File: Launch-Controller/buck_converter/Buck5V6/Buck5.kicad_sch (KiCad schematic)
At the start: 13 parts, among them J1 Conn_01x10_Socket, U1 LM2596S-5

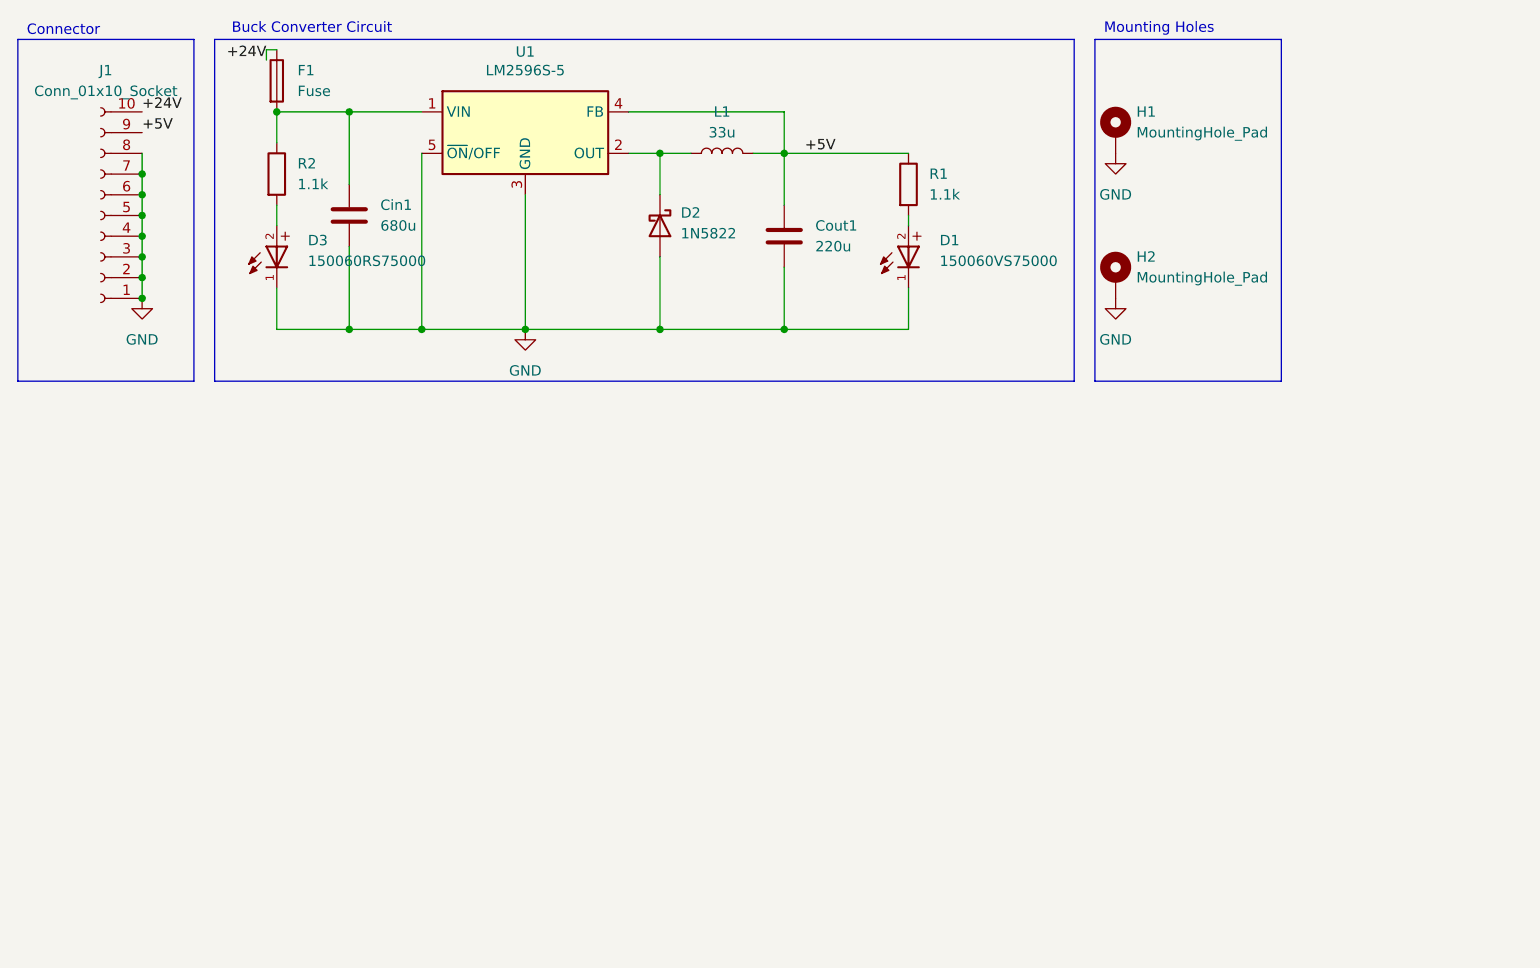
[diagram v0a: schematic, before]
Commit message: buck converter v2 changes
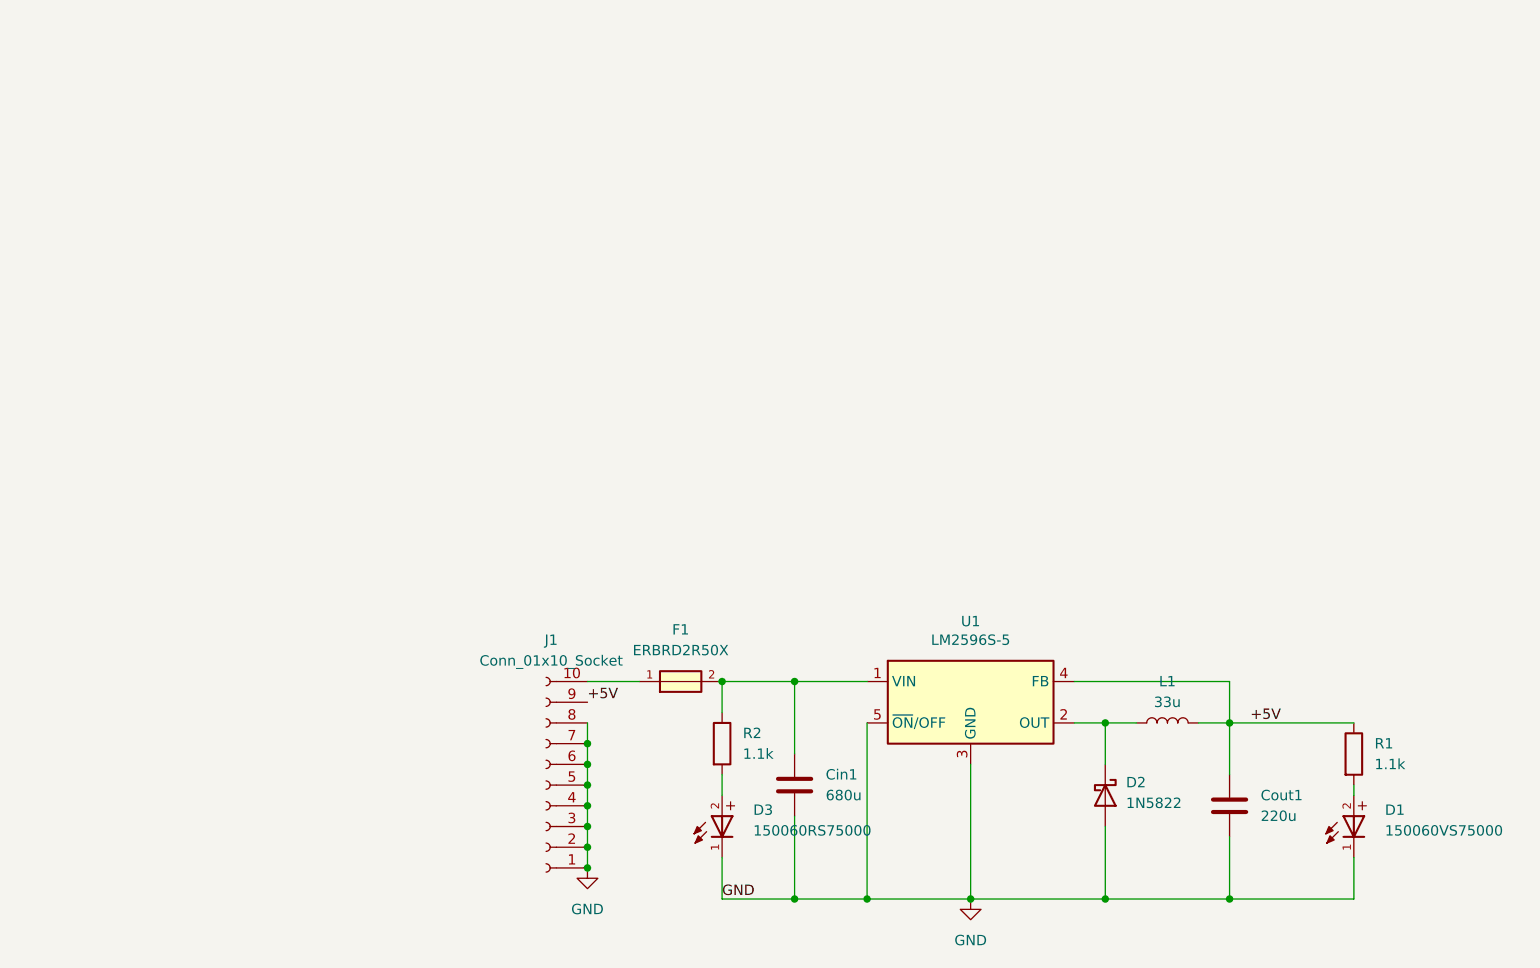
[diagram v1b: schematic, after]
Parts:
- removed F1: Fuse, Diode_SMD:D_0402_1005Metric_Pad0.77x0.64mm_HandSolder, symbol Device:Fuse
- removed H1, H2: MountingHole_Pad, MountingHole:MountingHole_3.7mm_Pad, symbol Mechanical:MountingHole_Pad
- added F1: ERBRD2R50X, Diode_SMD:D_0402_1005Metric_Pad0.77x0.64mm_HandSolder, symbol ERBRD2R50X:ERBRD2R50X
- Cin1: footprint KiCad:CAPAE660X800N -> 680_cap:CAP_FT_G_PAN
- Cout1: footprint footprints:CAP_YX_6P3X11_RUB -> 220_cap:CAP_YX_8X11P5_RUB
- L1: footprint NLCV32T_330K_EF:INDM3225X240N -> DR127_330_R1:IND_DR127-330-R_EAT
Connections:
- net at Cin1.1, R2.1, U1.1 (VIN): now also F1.2
- net +24V: no longer names the net of J1.10 (Pin_10)
- net +24V: now also F1.1
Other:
- note removed: "Buck Converter Circuit"
- note removed: "Connector"
- note removed: "Mounting Holes"
- moved on the sheet: Cin1, Cout1, D1, D2, D3, J1, L1, R1, R2, U1
